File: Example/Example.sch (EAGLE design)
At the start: 9 parts, among them IC1 LM555D, J1 UX60-MB-5S8, SW1 MFS101D-6-Z

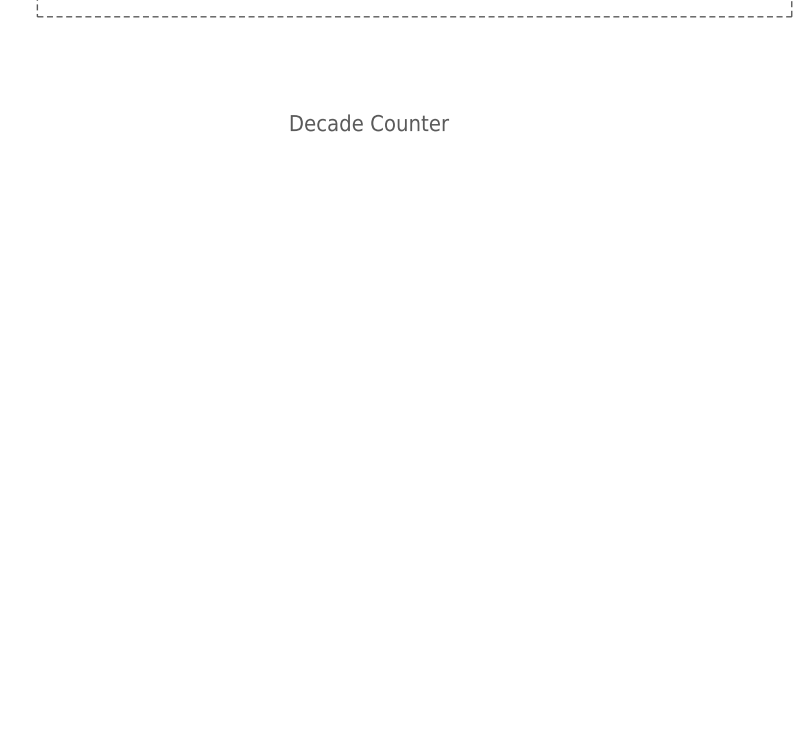
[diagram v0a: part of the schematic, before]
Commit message: added four new parts
added button, cell, led, and nor gate
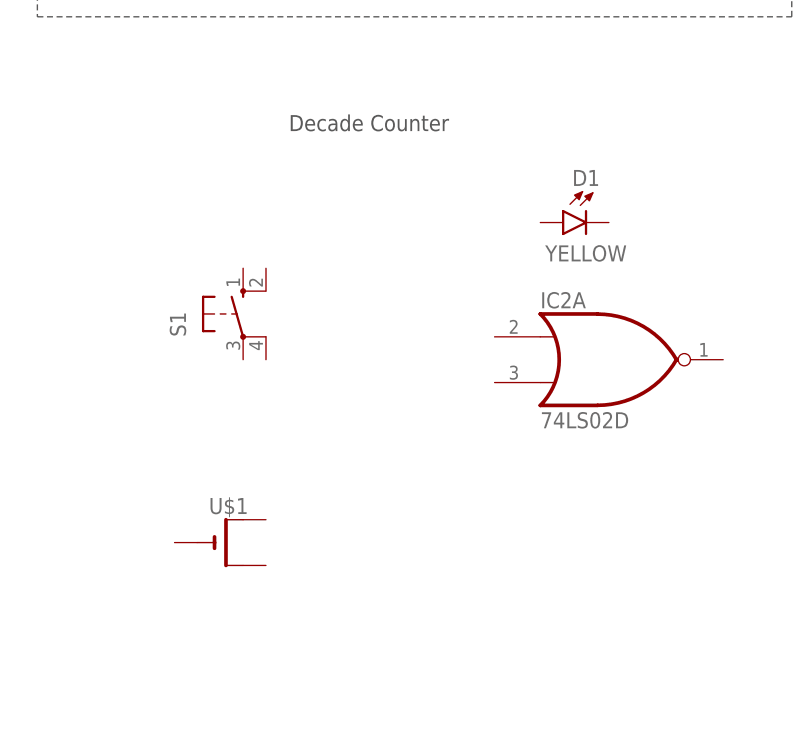
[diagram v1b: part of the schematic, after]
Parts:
- added D1: YELLOW, RoboJackets-LEDs:LED-SMD-YELLOW
- added IC2: 74LS02D, 74xx-us:74LS02D
- added S1: (no value), adafruit:40-XX-ROUND
- added U$1: (no value), adafruit:CR1220SMT
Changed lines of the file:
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@@
 <part name="SUPPLY12" library="RoboJackets-Supplies" deviceset="GND" device=""/>
 <part name="SW1" library="Example" deviceset="MFS101D-6-Z" device="" override_package3d_urn="urn:adsk.eagle:package:25000897/2" override_package_urn="urn:adsk.eagle:footprint:25000899/1"/>
+<part name="D1" library="RoboJackets-LEDs" deviceset="LED-SMD" device="" technology="-YELLOW" value="YELLOW"/>
+<part name="IC2" library="74xx-us" library_urn="urn:adsk.eagle:library:88" deviceset="74*02" device="D" package3d_urn="urn:adsk.eagle:package:2917/1" technology="LS"/>
+<part name="S1" library="adafruit" library_urn="urn:adsk.eagle:library:420" deviceset="40-XX" device="-ROUND" package3d_urn="urn:adsk.eagle:package:6240926/1"/>
+<part name="U$1" library="adafruit" library_urn="urn:adsk.eagle:library:420" deviceset="CR1220" device="SMT" package3d_urn="urn:adsk.eagle:package:6240665/1"/>
 </parts>
 <sheets>
@@
 <attribute name="VALUE" x="107.696" y="154.178" size="1.778" layer="96" rot="R180"/>
 </instance>
+<instance part="D1" gate="A" x="205.74" y="104.14" smashed="yes">
+<attribute name="NAME" x="205.74" y="108.204" size="1.778" layer="95" rot="MR0" align="bottom-center"/>
+<attribute name="VALUE" x="205.74" y="101.6" size="1.778" layer="96" rot="MR0" align="top-center"/>
+</instance>
+<instance part="IC2" gate="A" x="208.28" y="88.9" smashed="yes">
+<attribute name="NAME" x="200.66" y="94.615" size="1.778" layer="95"/>
+<attribute name="VALUE" x="200.66" y="81.28" size="1.778" layer="96"/>
+</instance>
+<instance part="S1" gate="1" x="167.64" y="93.98" smashed="yes">
+<attribute name="NAME" x="161.29" y="91.44" size="1.778" layer="95" rot="R90"/>
+<attribute name="VALUE" x="163.83" y="97.155" size="1.778" layer="96" rot="R90"/>
+</instance>
+<instance part="U$1" gate="G$1" x="165.1" y="68.58" smashed="yes">
+<attribute name="NAME" x="163.83" y="71.755" size="1.778" layer="95"/>
+<attribute name="VALUE" x="163.83" y="63.5" size="1.778" layer="96"/>
+</instance>
 </instances>

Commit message: sr latch
finished sr latch
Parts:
- removed D1: YELLOW, RoboJackets-LEDs:LED-SMD-YELLOW
- added D2, D3: YELLOW, RoboJackets-LEDs:LED-SMD-YELLOW
- added IC3: 74LS02D, 74xx-us:74LS02D
- added R1, R2, R3: (no value), rcl:R-US_R0603
- added S2: (no value), adafruit:40-XX-ROUND
- added U$3: (no value), adafruit:CR1220SMT
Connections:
- new net N$2: D3.A
- new net N$5: D3.C, R3.2
- new net Q: IC2A.O, IC3A.I0
- new net QNOT: IC2A.I1, IC3A.O
- new net R: IC2A.I0, R1.2, S1.S1
- new net S: IC3A.I1, R2.2, S2.S1
- new net VCC: S1.P, S2.P, U$1.+, U$3.+
- net GND: now also R1.1, R2.1, R3.1, U$1.-, U$3.-
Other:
- moved on the sheet: IC2A, S1, U$1
